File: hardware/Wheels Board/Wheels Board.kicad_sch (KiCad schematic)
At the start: 29 parts, among them J1 Conn_01x05, J2 Conn_01x05, J3 Conn_01x03, J4 53307-2471, J5 MX150_02x02_Vertical, U1 ASM330LHHTR, U2 XIAO-ESP32-S3-SMD, U3 TLV9001IDCK

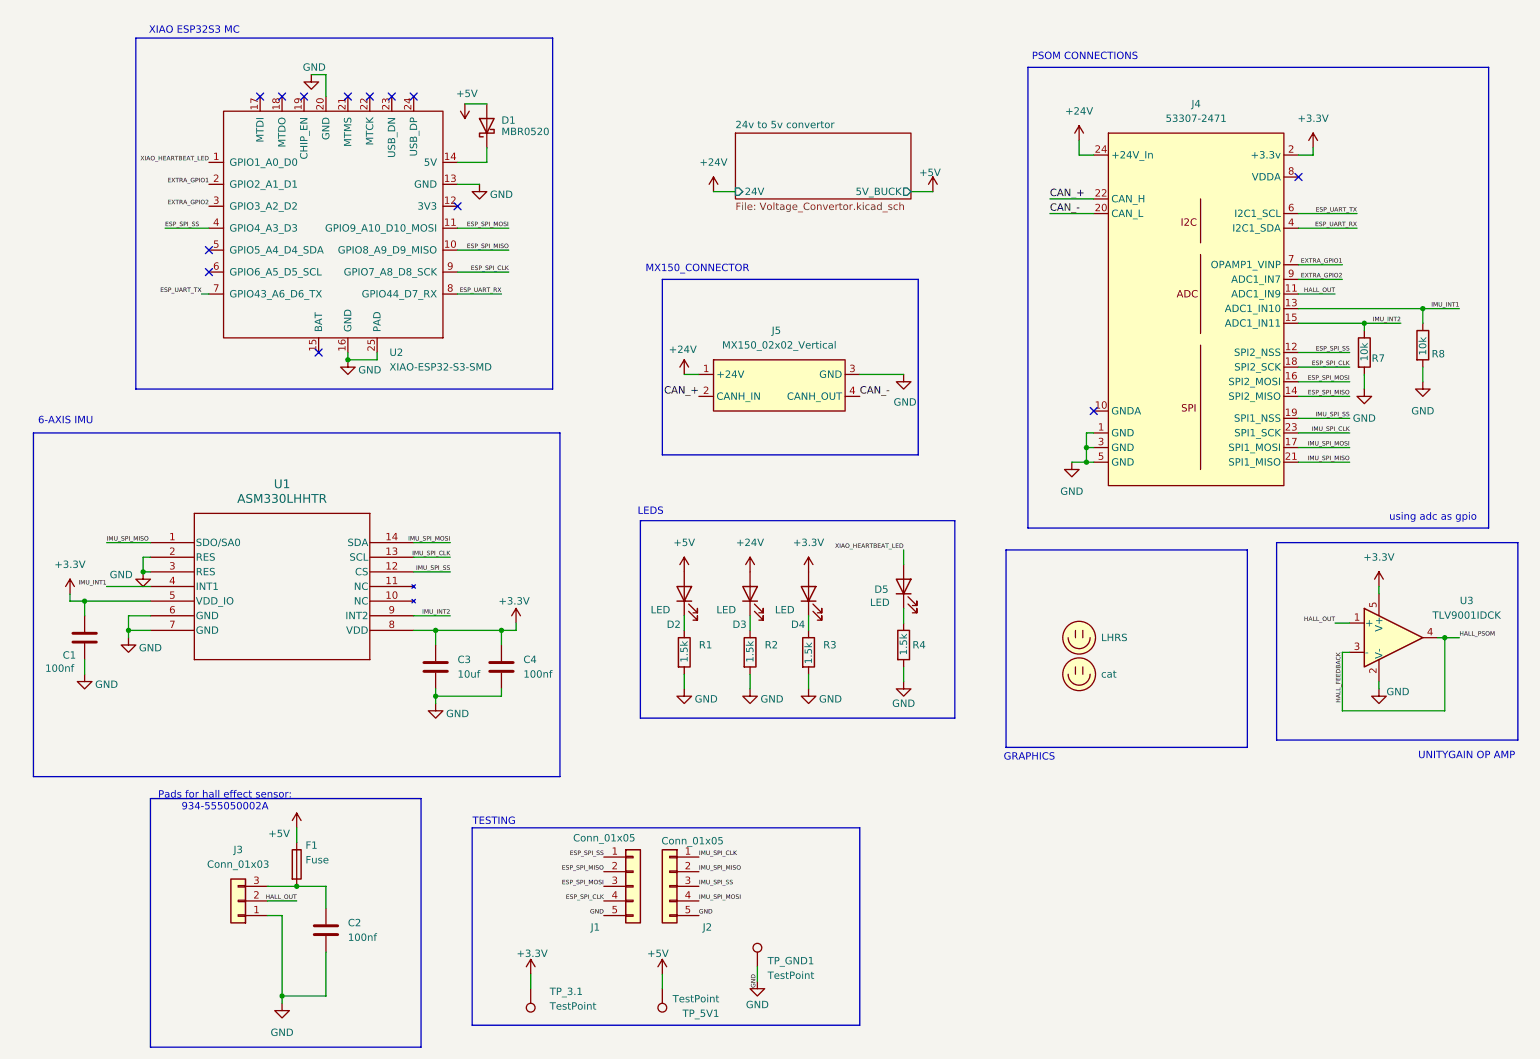
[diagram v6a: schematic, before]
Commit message: pre-2.4mm connector experiment
(will jump back to this if all goes wrong)
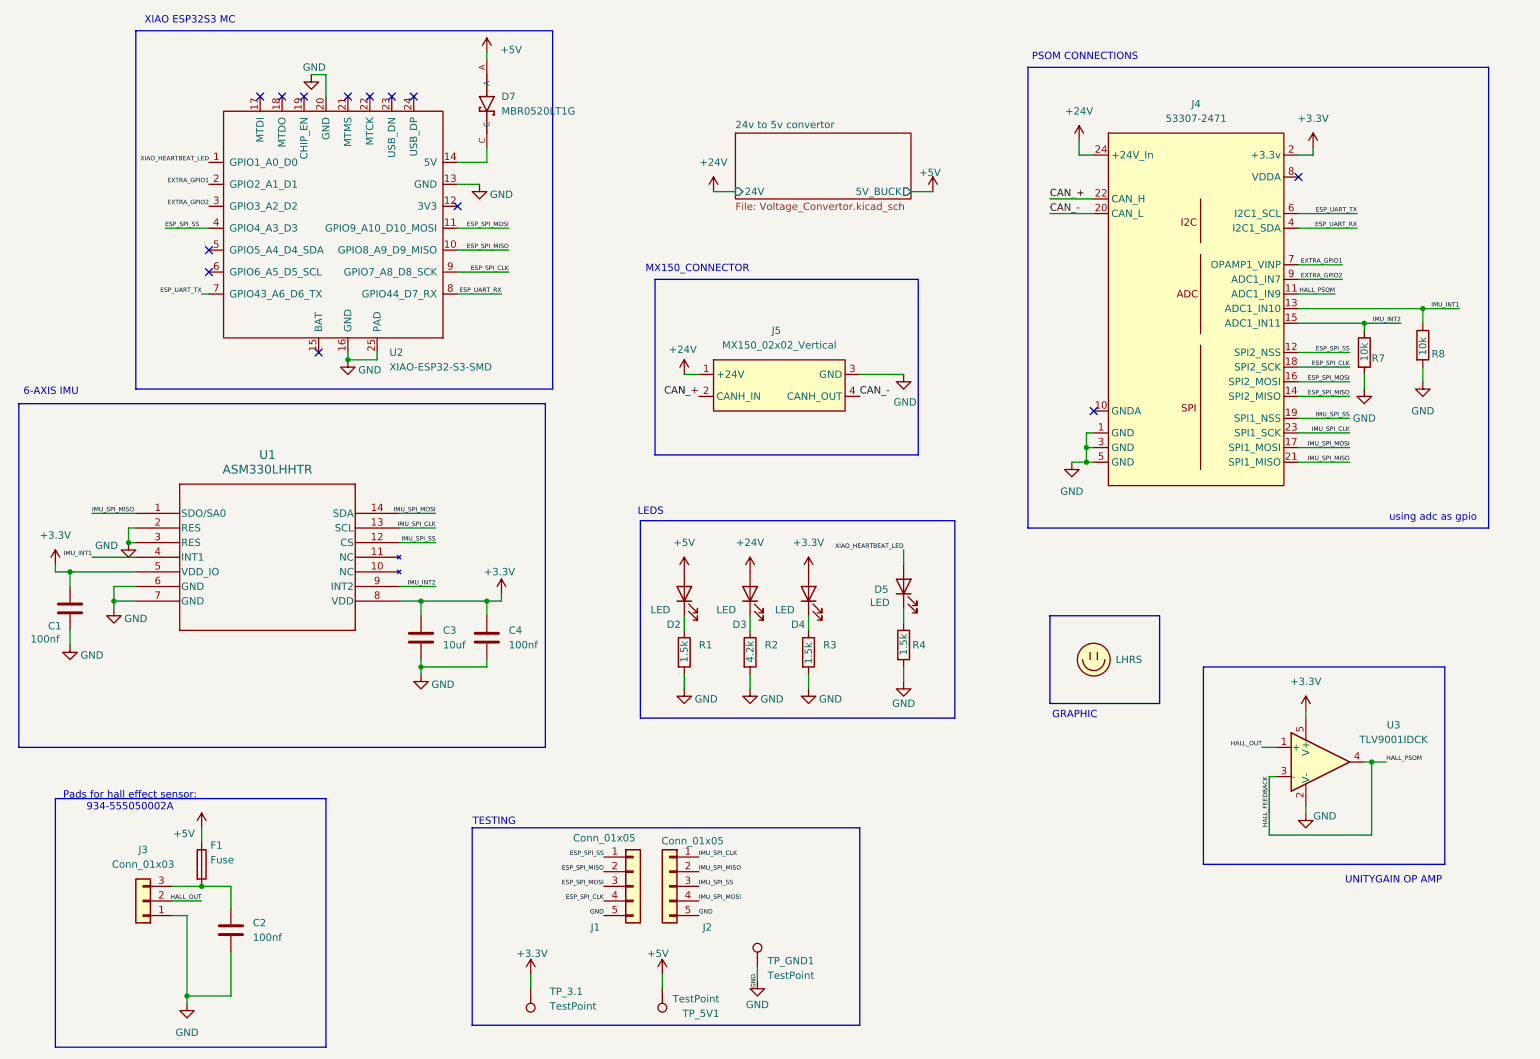
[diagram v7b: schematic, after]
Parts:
- removed D1: MBR0520, Diode_SMD:D_SOD-323_HandSoldering, symbol Diode:MBR0520
- removed LOGO2: cat, symbol utsvt_misc:Logo_Placeholder
- added D7: MBR0520LT1G, diode:SOD3716X135N, symbol MBR0520LT1G (diode):MBR0520LT1G
- R2: value 1.5k -> 4.2k
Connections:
- net +5V: now also D7.A
- net HALL_FEEDBACK: now also J4.11 (ADC1_IN9)
- net HALL_OUT: no longer J4.11 (ADC1_IN9)
- net at U2.14 (5V): now also D7.C
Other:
- note added: "GRAPHIC"
- note removed: "GRAPHICS"
- moved on the sheet: C1, C2, C3, C4, F1, J3, U1, U3

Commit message: pls pls pls
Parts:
- J1, J2: footprint Connector_PinHeader_1.00mm:PinHeader_1x05_P1.00mm_Vertical -> Connector_PinHeader_2.54mm:PinHeader_1x05_P2.54mm_Vertical
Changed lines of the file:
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@@
 			)
 		)
-		(property "Footprint" "Connector_PinHeader_1.00mm:PinHeader_1x05_P1.00mm_Vertical"
+		(property "Footprint" "Connector_PinHeader_2.54mm:PinHeader_1x05_P2.54mm_Vertical"
 			(at 129.54 165.1 0)
 			(effects
@@
 			)
 		)
-		(property "Footprint" "Connector_PinHeader_1.00mm:PinHeader_1x05_P1.00mm_Vertical"
+		(property "Footprint" "Connector_PinHeader_2.54mm:PinHeader_1x05_P2.54mm_Vertical"
 			(at 135.89 165.1 0)
 			(effects
